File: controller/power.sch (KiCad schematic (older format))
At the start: 2 parts

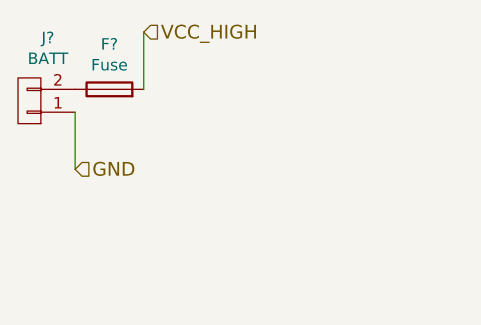
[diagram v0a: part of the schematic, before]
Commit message: Add more stuff to controller, start sourcing parts
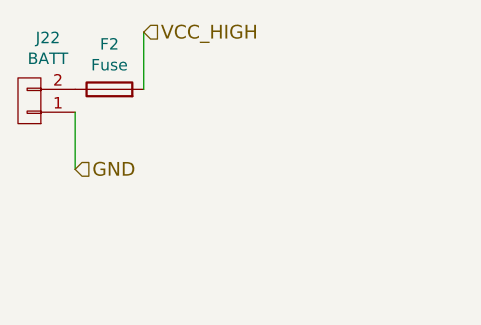
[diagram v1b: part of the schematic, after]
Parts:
- gave numbers to parts that had none: 2
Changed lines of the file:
@@
 LIBS:mic-parts
 LIBS:controller-cache
-LIBS:line-interface-cache
 EELAYER 26 0
 EELAYER END
 $Descr A4 11693 8268
 encoding utf-8
-Sheet 5 6
+Sheet 4 10
 Title ""
 Date ""
@@
 $EndDescr
 $Comp
-L CONN_01X02 J?
+L CONN_01X02 J22
 U 1 1 58C0B3B4
 P 900 1650
-F 0 "J?" H 819 1375 50  0000 C CNN
+F 0 "J22" H 819 1375 50  0000 C CNN
 F 1 "BATT" H 819 1466 50  0000 C CNN
 F 2 "" H -600 -1600 50  0001 C CNN
@@
 GND
 $Comp
-L Fuse F?
+L Fuse F2
 U 1 1 58C0B526
 P 1250 1600
-F 0 "F?" V 1447 1600 50  0000 C CNN
+F 0 "F2" V 1447 1600 50  0000 C CNN
 F 1 "Fuse" V 1356 1600 50  0000 C CNN
 F 2 "" V -1770 -50 50  0001 C CNN

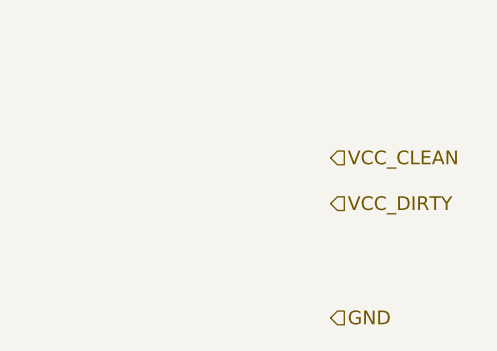
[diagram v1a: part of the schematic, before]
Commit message: Change gas pedal interface so that it supports going up and down from the middle voltage so that it's compatible with Linde forklift gas mechanism
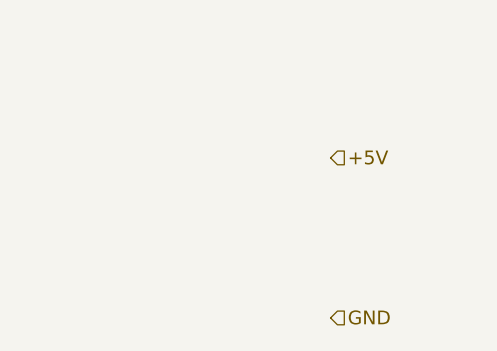
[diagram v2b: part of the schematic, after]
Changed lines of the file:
@@
 $EndComp
 Text HLabel 6700 1900 2    60   Input ~ 0
-VCC_CLEAN
-Text HLabel 6700 2100 2    60   Input ~ 0
-VCC_DIRTY
++5V
 Text HLabel 1400 1350 2    60   Input ~ 0
 VCC_HIGH

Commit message: More or less final controller board
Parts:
- added C36, C38: 1u, Capacitors_SMD:C_1210_HandSoldering, symbol C
- added C37: 470u, Capacitors_ThroughHole:CP_Radial_D16.0mm_P7.50mm, symbol CP1
- added C39: 1u, Capacitors_SMD:C_0603, symbol C
- added D34: D_TVS_ALT, Diodes_SMD:Diode-SMC_Handsoldering, symbol D_TVS_ALT
- added D52, D53: 16V, Diodes_SMD:D_SMB_Handsoldering, symbol D_Zener
- added D54: D, Diodes_SMD:D_SOD-123, symbol D
- added D55: GREEN, LEDs:LED_0603, symbol LED_ALT
- added MK5, MK6, MK7, MK8: Mounting_Hole, Mounting_Holes:MountingHole_3.2mm_M3, symbol Mounting_Hole
- added Q8: NDT2955, TO_SOT_Packages_SMD:TO-252-2Lead, symbol Q_PMOS_GSD
- added R60: 10k, Resistors_SMD:R_0603, symbol R
- added R61: 10, Resistors_SMD:R_0805_HandSoldering, symbol R
- added R62: 330, Resistors_SMD:R_0603, symbol R
- added U5: LM7805CT, TO_SOT_Packages_SMD:TO-252-2Lead, symbol LM7805CT
- F2: footprint (none) -> smalsiukas-footpints:Automotive-Fuse-Holder; Distributor (none) -> 1586596; Manufacturer (none) -> ?; PartNo (none) -> ?
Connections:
- net +5V: now also C39.1, D54.2 (A), R62.1, U5.3 (OUT)
- net GND: now also C36.2, C37.2, C38.2, C39.2, D34.2 (A2), D53.2 (A), D55.1 (K), R60.1, U5.2 (GND)
- net VCC_HIGH renamed VCC
- net VCC: now also C36.1, D34.1 (A1), Q8.3 (D)
- new net: C37.1, C38.1, D53.1 (K), D54.1 (K), R61.2, U5.1 (IN)
- new net: D52.2 (A), Q8.1 (G), R60.2
- new net: D52.1 (K), Q8.2 (S), R61.1
- new net: D55.2 (A), R62.2
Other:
- moved on the sheet: F2, J22

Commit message: Finish the routing, add some significant fixes: *correct to-252 pin numbering * longer pads for relays * fix footprint of the optocouplers
Also finish the routing
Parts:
- added U16: LM7805CT, TO_SOT_Packages_THT:TO-220_Vertical, symbol LM7805CT
- D34: Distributor 2536658 -> 2536498
- D55: footprint LEDs:LED_0603 -> LEDs:LED_D5.0mm
- J22: footprint (none) -> Connectors_Terminal_Blocks:TerminalBlock_Pheonix_MKDS1.5-2pol; Distributor (none) -> ?; Manufacturer (none) -> ?; PartNo (none) -> ?
- Q8: symbol Q_PMOS_GSD -> Q_NMOS_GDS
- R60: footprint Resistors_SMD:R_0603 -> Resistors_SMD:R_0603_HandSoldering; Distributor (none) -> ?; Manufacturer (none) -> ?; PartNo (none) -> ?
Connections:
- net GND: now also J22.2 (P2), U16.2 (GND); no longer J22.1 (P1)
- net VCC: now also D52.1 (K), R61.1; no longer C36.1, D34.1 (A1), F2.2
- net at F2.1: now also J22.1 (P1); no longer J22.2 (P2)
- net at C37.1, C38.1, D53.1 (K)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: now also U16.1 (IN)
- new net: C36.1, D34.1 (A1), F2.2, Q8.2 (D)
- new net +5V_DIRTY: U16.3 (OUT)
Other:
- note added: "Saugikliai: 2137122\n"
- moved on the sheet: C38, C39, D54, D55, R62, U5
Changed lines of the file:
@@
 F 0 "J22" H 2319 3225 50  0000 C CNN
 F 1 "BATT" H 2319 3316 50  0000 C CNN
-F 2 "" H 900 250 50  0001 C CNN
+F 2 "Connectors_Terminal_Blocks:TerminalBlock_Pheonix_MKDS1.5-2pol" H 900 250 50  0001 C CNN
 F 3 "" H 900 250 50  0001 C CNN
+F 4 "?" H 2400 3500 60  0001 C CNN "PartNo"
+F 5 "?" H 2400 3500 60  0001 C CNN "Manufacturer"
+F 6 "?" H 2400 3500 60  0001 C CNN "Distributor"
 	1    2400 3500
-	-1   0    0    1
-$EndComp
-Text HLabel 7950 3450 2    60   Input ~ 0
+	-1   0    0    -1
+$EndComp
+Text HLabel 8550 3450 2    60   Input ~ 0
 +5V
-Text HLabel 2900 3150 2    60   Input ~ 0
+Text HLabel 5000 3150 2    60   Input ~ 0
 VCC_HIGH
-Text HLabel 7950 4250 2    60   Input ~ 0
+Text HLabel 8550 4250 2    60   Input ~ 0
 GND
 $Comp
@@
 	2600 3800 2600 3550
 Wire Wire Line
-	2900 3150 2900 3450
+	5000 3150 5000 3450
 $Comp
 L VCC #PWR012
 U 1 1 58C97562
-P 3850 3150
-F 0 "#PWR012" H 3850 3000 60  0001 C CNN
-F 1 "VCC" H 3850 3300 60  0000 C CNN
-F 2 "" H 3850 3150 60  0000 C CNN
-F 3 "" H 3850 3150 60  0000 C CNN
-	1    3850 3150
-	1    0    0    -1
-$EndComp
-Connection ~ 6300 3450
+P 5000 3150
+F 0 "#PWR012" H 5000 3000 60  0001 C CNN
+F 1 "VCC" H 5000 3300 60  0000 C CNN
+F 2 "" H 5000 3150 60  0000 C CNN
+F 3 "" H 5000 3150 60  0000 C CNN
+	1    5000 3150
+	1    0    0    -1
+$EndComp
+Connection ~ 6900 3450
 $Comp
 L C C38
 U 1 1 58C97572
-P 6300 3600
-F 0 "C38" H 6350 3700 50  0000 L CNN
-F 1 "1u" H 6350 3500 50  0000 L CNN
-F 2 "Capacitors_SMD:C_1210_HandSoldering" H 6338 3450 30  0001 C CNN
-F 3 "" H 6300 3600 60  0000 C CNN
-F 4 "?" H 6300 3600 60  0001 C CNN "PartNo"
-F 5 "?" H 6300 3600 60  0001 C CNN "Manufacturer"
-F 6 "2320928" H 6300 3600 60  0001 C CNN "Distributor"
-	1    6300 3600
+P 6900 3600
+F 0 "C38" H 6950 3700 50  0000 L CNN
+F 1 "1u" H 6950 3500 50  0000 L CNN
+F 2 "Capacitors_SMD:C_1210_HandSoldering" H 6938 3450 30  0001 C CNN
+F 3 "" H 6900 3600 60  0000 C CNN
+F 4 "?" H 6900 3600 60  0001 C CNN "PartNo"
+F 5 "?" H 6900 3600 60  0001 C CNN "Manufacturer"
+F 6 "2320928" H 6900 3600 60  0001 C CNN "Distributor"
+	1    6900 3600
 	-1   0    0    -1
 $EndComp
@@
 L C C39
 U 1 1 58C97574
-P 7500 3600
-F 0 "C39" H 7550 3700 50  0000 L CNN
-F 1 "1u" H 7550 3500 50  0000 L CNN
-F 2 "Capacitors_SMD:C_0603" H 7538 3450 30  0001 C CNN
-F 3 "" H 7500 3600 60  0000 C CNN
-	1    7500 3600
-	1    0    0    -1
-$EndComp
-Wire Wire Line
-	7100 3450 7950 3450
-Connection ~ 6700 4250
-Wire Wire Line
-	7500 4250 7500 3750
-Wire Wire Line
-	7500 3450 7500 3300
-$Comp
-L Q_PMOS_GSD Q8
+P 8100 3600
+F 0 "C39" H 8150 3700 50  0000 L CNN
+F 1 "1u" H 8150 3500 50  0000 L CNN
+F 2 "Capacitors_SMD:C_0603" H 8138 3450 30  0001 C CNN
+F 3 "" H 8100 3600 60  0000 C CNN
+	1    8100 3600
+	1    0    0    -1
+$EndComp
+Wire Wire Line
+	7700 3450 8550 3450
+Connection ~ 7300 4250
+Wire Wire Line
+	8100 4250 8100 3750
+Wire Wire Line
+	8100 3450 8100 3300
+$Comp
+L Q_NMOS_GDS Q8
 U 1 1 58C97575
 P 4550 3550
 F 0 "Q8" V 4878 3550 50  0000 C CNN
 F 1 "NDT2955" V 4787 3550 50  0000 C CNN
-F 2 "TO_SOT_Packages_SMD:TO-252-2Lead" V 4950 3300 29  0000 C CNN
+F 2 "TO_SOT_Packages_SMD:TO-252-2Lead" V 4950 3700 29  0000 C CNN
 F 3 "" H 6850 2800 60  0000 C CNN
 F 4 "IRFR5410TRPBF" H 4550 3550 60  0001 C CNN "PartNo"
@@
 	4750 3450 5150 3450
 Wire Wire Line
-	5450 3450 6300 3450
-Wire Wire Line
-	3850 3150 3850 3700
-Connection ~ 6300 4250
+	5450 3450 6900 3450
+Connection ~ 6900 4250
 Connection ~ 4550 4250
 Wire Wire Line
-	3850 4250 7950 4250
-Wire Wire Line
-	6300 3750 6300 4250
-Wire Wire Line
-	6700 3750 6700 4250
+	3850 4250 8550 4250
+Wire Wire Line
+	6900 3750 6900 4250
+Wire Wire Line
+	7300 3750 7300 4250
 $Comp
 L +5V #PWR013
 U 1 1 58C9757F
-P 7500 3300
-F 0 "#PWR013" H 1550 1950 50  0001 C CNN
-F 1 "+5V" H 7515 3473 50  0000 C CNN
-F 2 "" H 1550 2100 50  0001 C CNN
-F 3 "" H 1550 2100 50  0001 C CNN
-	1    7500 3300
+P 8100 3300
+F 0 "#PWR013" H 2150 1950 50  0001 C CNN
+F 1 "+5V" H 8115 3473 50  0000 C CNN
+F 2 "" H 2150 2100 50  0001 C CNN
+F 3 "" H 2150 2100 50  0001 C CNN
+	1    8100 3300
 	1    0    0    -1
 $EndComp
@@
 F 0 "R60" V 4630 3900 50  0000 C CNN
 F 1 "10k" V 4557 3901 50  0000 C CNN
-F 2 "Resistors_SMD:R_0603" V 4480 3900 30  0001 C CNN
+F 2 "Resistors_SMD:R_0603_HandSoldering" V 4480 3900 30  0001 C CNN
 F 3 "" H 4550 3900 30  0000 C CNN
+F 4 "?" H 4550 3900 60  0001 C CNN "PartNo"
+F 5 "?" H 4550 3900 60  0001 C CNN "Manufacturer"
+F 6 "?" H 4550 3900 60  0001 C CNN "Distributor"
 	1    4550 3900
 	-1   0    0    1
@@
 	4550 3750 5000 3750
 Connection ~ 4550 3750
-Connection ~ 7100 3450
+Connection ~ 7700 3450
 $Comp
 L D_TVS_ALT D34
@@
 F 4 "?" H 3850 3850 60  0001 C CNN "PartNo"
 F 5 "WURTH" H 3850 3850 60  0001 C CNN "Manufacturer"
-F 6 "2536658" H 3850 3850 60  0001 C CNN "Distributor"
+F 6 "2536498" H 3850 3850 60  0001 C CNN "Distributor"
 	1    3850 3850
 	0    -1   1    0
@@
 L LED_ALT D55
 U 1 1 58C9758A
-P 7950 3950
-F 0 "D55" V 7988 3832 50  0000 R CNN
-F 1 "GREEN" V 7897 3832 50  0000 R CNN
-F 2 "LEDs:LED_0603" H 3800 300 50  0001 C CNN
-F 3 "" H 3800 300 50  0001 C CNN
-F 4 "?" H 7950 3950 60  0001 C CNN "PartNo"
-F 5 "?" H 7950 3950 60  0001 C CNN "Manufacturer"
-F 6 "?" H 7950 3950 60  0001 C CNN "Distributor"
-	1    7950 3950
+P 8550 3950
+F 0 "D55" V 8588 3832 50  0000 R CNN
+F 1 "GREEN" V 8497 3832 50  0000 R CNN
+F 2 "LEDs:LED_D5.0mm" H 4400 300 50  0001 C CNN
+F 3 "" H 4400 300 50  0001 C CNN
+F 4 "?" H 8550 3950 60  0001 C CNN "PartNo"
+F 5 "?" H 8550 3950 60  0001 C CNN "Manufacturer"
+F 6 "?" H 8550 3950 60  0001 C CNN "Distributor"
+	1    8550 3950
 	0    -1   -1   0
 $EndComp
 Wire Wire Line
-	7950 4250 7950 4100
-Connection ~ 7500 4250
+	8550 4250 8550 4100
+Connection ~ 8100 4250
 $Comp
 L R R62
 U 1 1 58C9758B
-P 7950 3650
-F 0 "R62" V 8030 3650 50  0000 C CNN
-F 1 "330" V 7957 3651 50  0000 C CNN
-F 2 "Resistors_SMD:R_0603" V 7880 3650 30  0001 C CNN
-F 3 "" H 7950 3650 30  0000 C CNN
-	1    7950 3650
+P 8550 3650
+F 0 "R62" V 8630 3650 50  0000 C CNN
+F 1 "330" V 8557 3651 50  0000 C CNN
+F 2 "Resistors_SMD:R_0603" V 8480 3650 30  0001 C CNN
+F 3 "" H 8550 3650 30  0000 C CNN
+	1    8550 3650
 	-1   0    0    -1
 $EndComp
-Connection ~ 7500 3450
-Wire Wire Line
-	7950 3450 7950 3500
+Connection ~ 8100 3450
+Wire Wire Line
+	8550 3450 8550 3500
 Connection ~ 5000 3450
 $Comp
@@
 L D D54
 U 1 1 58C97593
-P 6700 3050
-F 0 "D54" H 6700 3266 50  0000 C CNN
-F 1 "D" H 6700 3175 50  0000 C CNN
-F 2 "Diodes_SMD:D_SOD-123" H 2400 2150 50  0001 C CNN
-F 3 "" H 2400 2150 50  0001 C CNN
-F 4 "?" H 6700 3050 60  0001 C CNN "PartNo"
-F 5 "?" H 6700 3050 60  0001 C CNN "Manufacturer"
-F 6 "?" H 6700 3050 60  0001 C CNN "Distributor"
-	1    6700 3050
-	1    0    0    -1
-$EndComp
-Wire Wire Line
-	6850 3050 7100 3050
-Wire Wire Line
-	6550 3050 6300 3050
-Wire Wire Line
-	6300 3050 6300 3450
+P 7300 3050
+F 0 "D54" H 7300 3266 50  0000 C CNN
+F 1 "D" H 7300 3175 50  0000 C CNN
+F 2 "Diodes_SMD:D_SOD-123" H 3000 2150 50  0001 C CNN
+F 3 "" H 3000 2150 50  0001 C CNN
+F 4 "?" H 7300 3050 60  0001 C CNN "PartNo"
+F 5 "?" H 7300 3050 60  0001 C CNN "Manufacturer"
+F 6 "?" H 7300 3050 60  0001 C CNN "Distributor"
+	1    7300 3050
+	1    0    0    -1
+$EndComp
+Wire Wire Line
+	7450 3050 7700 3050
+Wire Wire Line
+	7150 3050 6900 3050
+Wire Wire Line
+	6900 3050 6900 3450
 Connection ~ 2900 3450
 $Comp
 L LM7805CT U5
 U 1 1 58C989E8
-P 6700 3500
-F 0 "U5" H 6700 3817 50  0000 C CNN
-F 1 "LM7805CT" H 6700 3726 50  0000 C CNN
-F 2 "TO_SOT_Packages_SMD:TO-252-2Lead" H 6700 3600 50  0001 C CIN
-F 3 "" H 6700 3500 50  0001 C CNN
-F 4 "KA7805ERTF" H 6700 3500 60  0001 C CNN "PartNo"
-F 5 "FAIRCHILD" H 6700 3500 60  0001 C CNN "Manufacturer"
-F 6 "2102585" H 6700 3500 60  0001 C CNN "Distributor"
-	1    6700 3500
-	1    0    0    -1
-$EndComp
-Wire Wire Line
-	7100 3050 7100 3450
+P 7300 3500
+F 0 "U5" H 7300 3817 50  0000 C CNN
+F 1 "LM7805CT" H 7300 3726 50  0000 C CNN
+F 2 "TO_SOT_Packages_SMD:TO-252-2Lead" H 7300 3600 50  0001 C CIN
+F 3 "" H 7300 3500 50  0001 C CNN
+F 4 "KA7805ERTF" H 7300 3500 60  0001 C CNN "PartNo"
+F 5 "FAIRCHILD" H 7300 3500 60  0001 C CNN "Manufacturer"
+F 6 "2102585" H 7300 3500 60  0001 C CNN "Distributor"
+	1    7300 3500
+	1    0    0    -1
+$EndComp
+Wire Wire Line
+	7700 3050 7700 3450
 $Comp
 L D_Zener D52
@@
 	1    0    0    -1
 $EndComp
+Wire Wire Line
+	3850 3700 3850 3450
+Text Notes 2400 3150 0    60   ~ 0
+Saugikliai: 2137122\n
+$Comp
+L LM7805CT U16
+U 1 1 58CC5716
+P 6950 5150
+F 0 "U16" H 6950 5467 50  0000 C CNN
+F 1 "LM7805CT" H 6950 5376 50  0000 C CNN
+F 2 "TO_SOT_Packages_THT:TO-220_Vertical" H 6950 5250 50  0001 C CIN
+F 3 "" H 6950 5150 50  0001 C CNN
+F 4 "OKI-78SR-5/1.5-W36-C" H 6950 5150 60  0001 C CNN "PartNo"
+F 5 "MURATA" H 6950 5150 60  0001 C CNN "Manufacturer"
+F 6 "2102101" H 6950 5150 60  0001 C CNN "Distributor"
+	1    6950 5150
+	1    0    0    -1
+$EndComp
+Wire Wire Line
+	6550 5100 6550 3450
+Connection ~ 6550 3450
+Wire Wire Line
+	6350 4250 6350 5400
+Wire Wire Line
+	6350 5400 6950 5400
+Connection ~ 6350 4250
+Wire Wire Line
+	7350 5100 8550 5100
+Text HLabel 8550 5100 2    60   Input ~ 0
++5V_DIRTY
 $EndSCHEMATC

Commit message: Update the 5 and 2 pin terminal footprints, shuffle around some tracks
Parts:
- J22: footprint Connectors_Terminal_Blocks:TerminalBlock_Pheonix_MKDS1.5-2pol -> smalsiukas-footpints:TerminalBlock_5.08-2pol
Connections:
- net GND: now also J22.1 (P1); no longer J22.2 (P2)
- net at F2.1: now also J22.2 (P2); no longer J22.1 (P1)
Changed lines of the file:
@@
 F 0 "J22" H 2319 3225 50  0000 C CNN
 F 1 "BATT" H 2319 3316 50  0000 C CNN
-F 2 "Connectors_Terminal_Blocks:TerminalBlock_Pheonix_MKDS1.5-2pol" H 900 250 50  0001 C CNN
+F 2 "smalsiukas-footpints:TerminalBlock_5.08-2pol" H 900 250 50  0001 C CNN
 F 3 "" H 900 250 50  0001 C CNN
 F 4 "?" H 2400 3500 60  0001 C CNN "PartNo"
@@
 F 6 "?" H 2400 3500 60  0001 C CNN "Distributor"
 	1    2400 3500
-	-1   0    0    -1
+	-1   0    0    1
 $EndComp
 Text HLabel 8550 3450 2    60   Input ~ 0

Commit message: Various fixes and comments to the controller board, also making it suitable for non-plated holes.
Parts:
- Q8: symbol Q_NMOS_GDS -> Q_PMOS_GDS
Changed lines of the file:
@@
 encoding utf-8
 Sheet 4 10
-Title "Digital soil moisture sensor"
-Date "Tue 17 Feb 2015"
-Rev ""
-Comp "Catnip electronics"
-Comment1 "by Albertas Mickėnas mic@wemakethings.net"
+Title "Smalsiukas - Toyota lifter hack"
+Date "2017-04-01"
+Rev "Rev1"
+Comp "TECHNARIUM"
+Comment1 "Albertas Mickėnas"
 Comment2 ""
 Comment3 ""
@@
 	8100 3450 8100 3300
 $Comp
-L Q_NMOS_GDS Q8
+L Q_PMOS_GDS Q8
 U 1 1 58C97575
 P 4550 3550
